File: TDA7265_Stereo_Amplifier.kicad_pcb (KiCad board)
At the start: 2 copper layers, 70.5 x 49 mm, 20 parts, among them J1 DC Jack, J2 ASJ-37A-5-M, J3 Output jack, U1 TDA7265

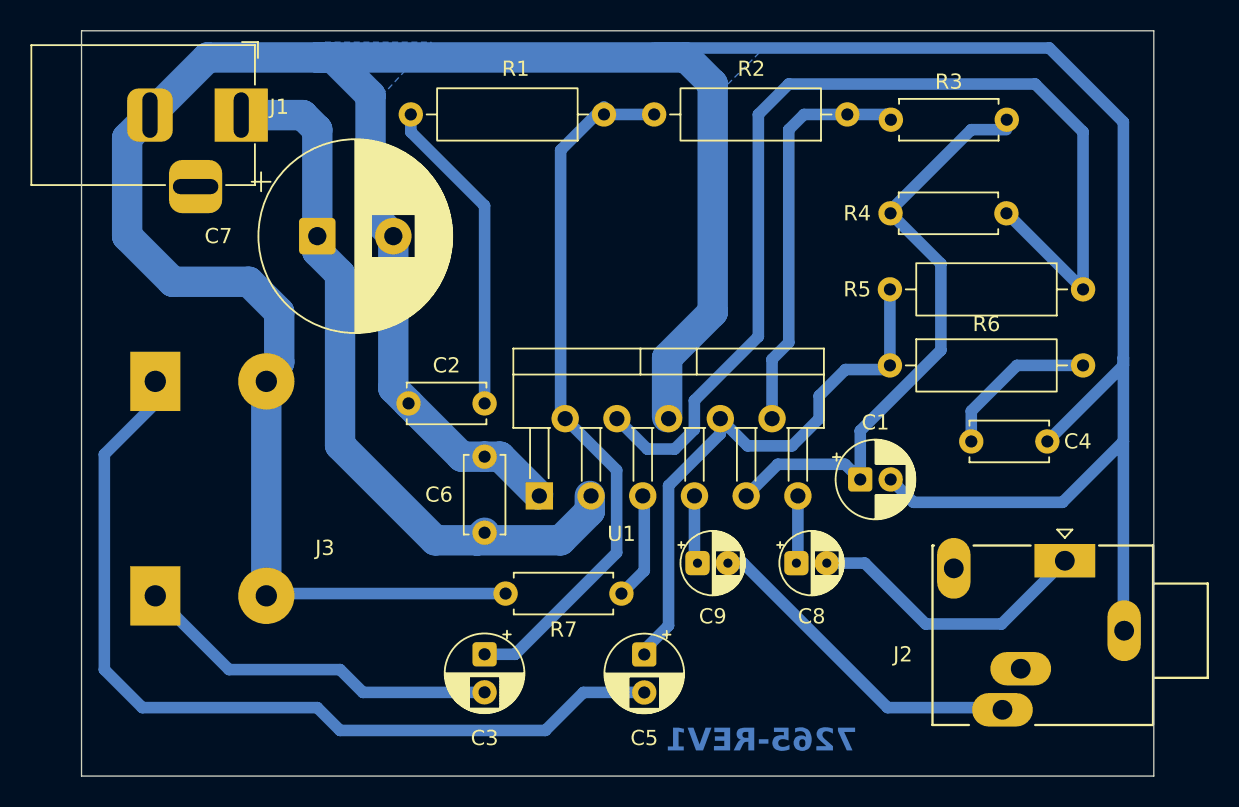
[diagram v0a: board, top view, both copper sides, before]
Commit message: Fix issue with right channel and create more space for heat sink
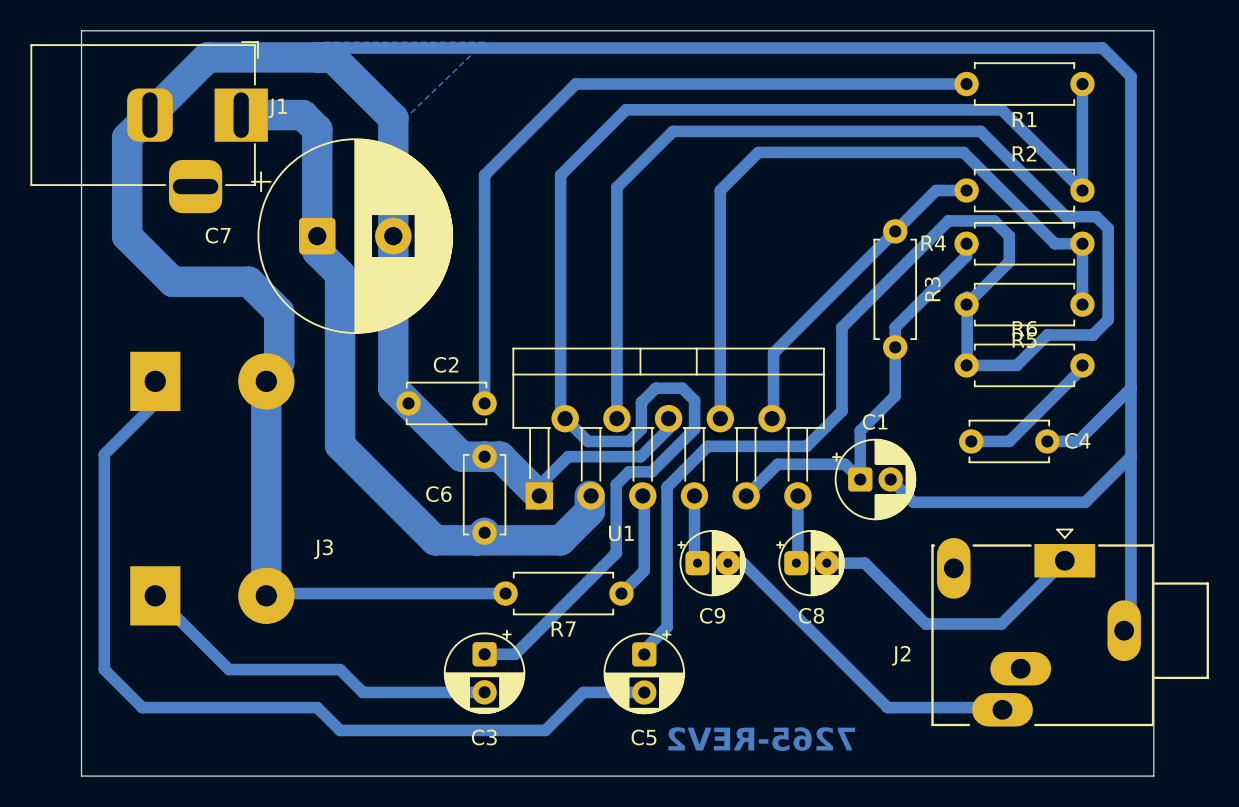
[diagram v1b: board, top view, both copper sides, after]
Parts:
- C7: value 1000uF -> 2200uF
- R1, R2, R5, R6: footprint Resistor_THT:R_Axial_DIN0309_L9.0mm_D3.2mm_P12.70mm_Horizontal -> Resistor_THT:R_Axial_DIN0207_L6.3mm_D2.5mm_P7.62mm_Horizontal
- moved R1 31.5 mm to (174.3, 73.0)
- moved R2 9.30 mm to (166.7, 80.0), turned to 0 degrees
- moved R3 7.35 mm to (162.0, 82.7), turned to -90 degrees
- moved R4 5.39 mm to (174.3, 83.5)
- moved R6 5.04 mm to (166.7, 91.5)
- moved R5 1.00 mm to (174.3, 87.5)
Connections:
- U1 pad 4: /OUTR+ -> /INR-
- U1 pad 8: /INR- -> /OUTR+
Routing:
- net /INR-: track 37.5 -> 123.4 mm
- net /OUTL-: track 46.8 -> 98.1 mm
- net Net-(C2-Pad1): track 21.0 -> 49.2 mm
- net /OUTR+: track 69.9 -> 47.2 mm
- net GND: track 248.5 -> 233.3 mm
- net GNDA: track 39.9 -> 27.2 mm
- net /INL-: track 26.7 -> 21.5 mm
- net Net-(C4-Pad1): track 10.6 -> 9.51 mm
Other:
- board text added: "7265-REV2"
- board text removed: "7265-REV1"
